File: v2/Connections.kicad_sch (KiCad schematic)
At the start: 11 parts, among them J3 Screw_Terminal_01x02, J4 Screw_Terminal_01x03, U10 TPD4E05U06DQA

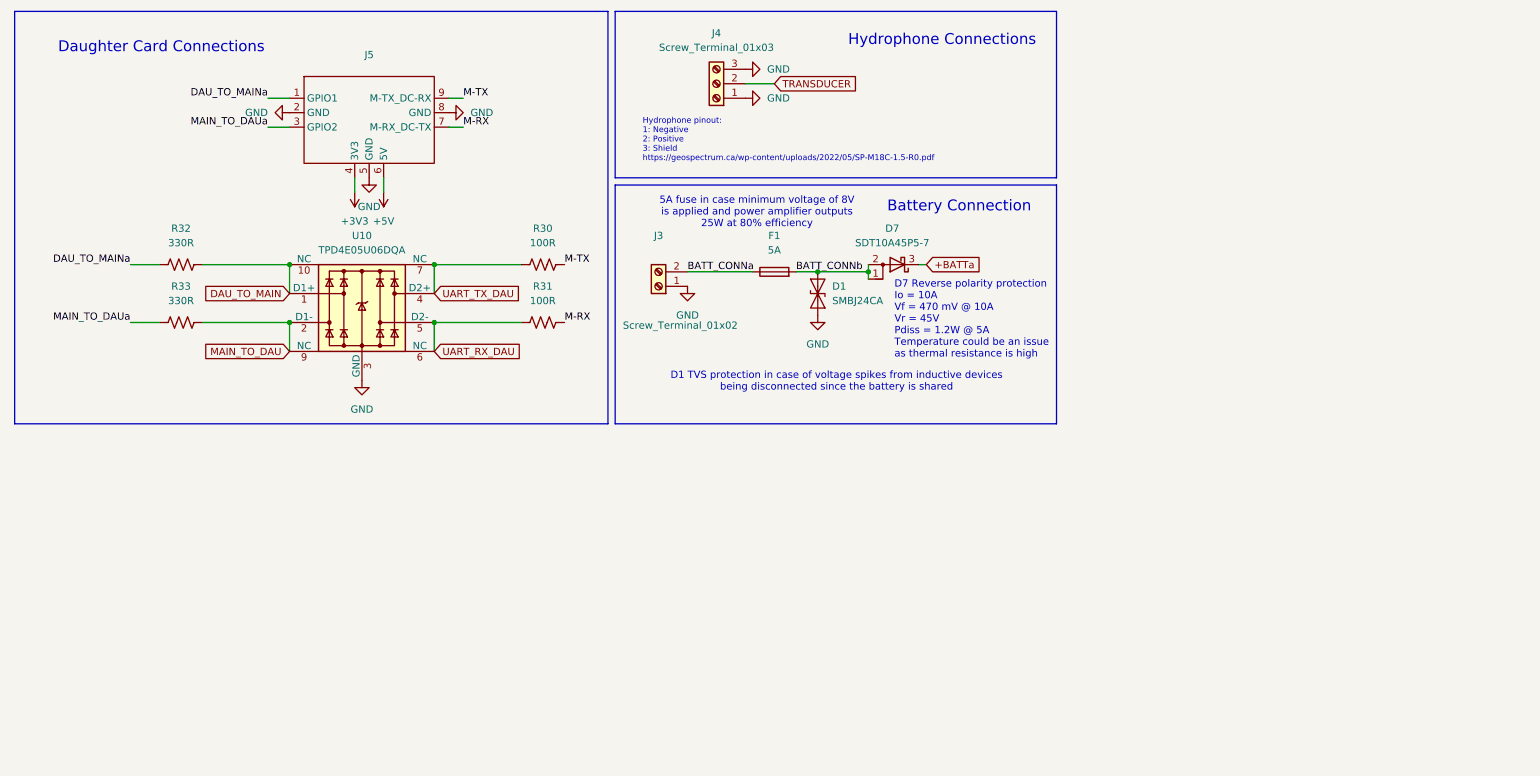
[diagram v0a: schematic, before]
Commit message: Most v2 changes made
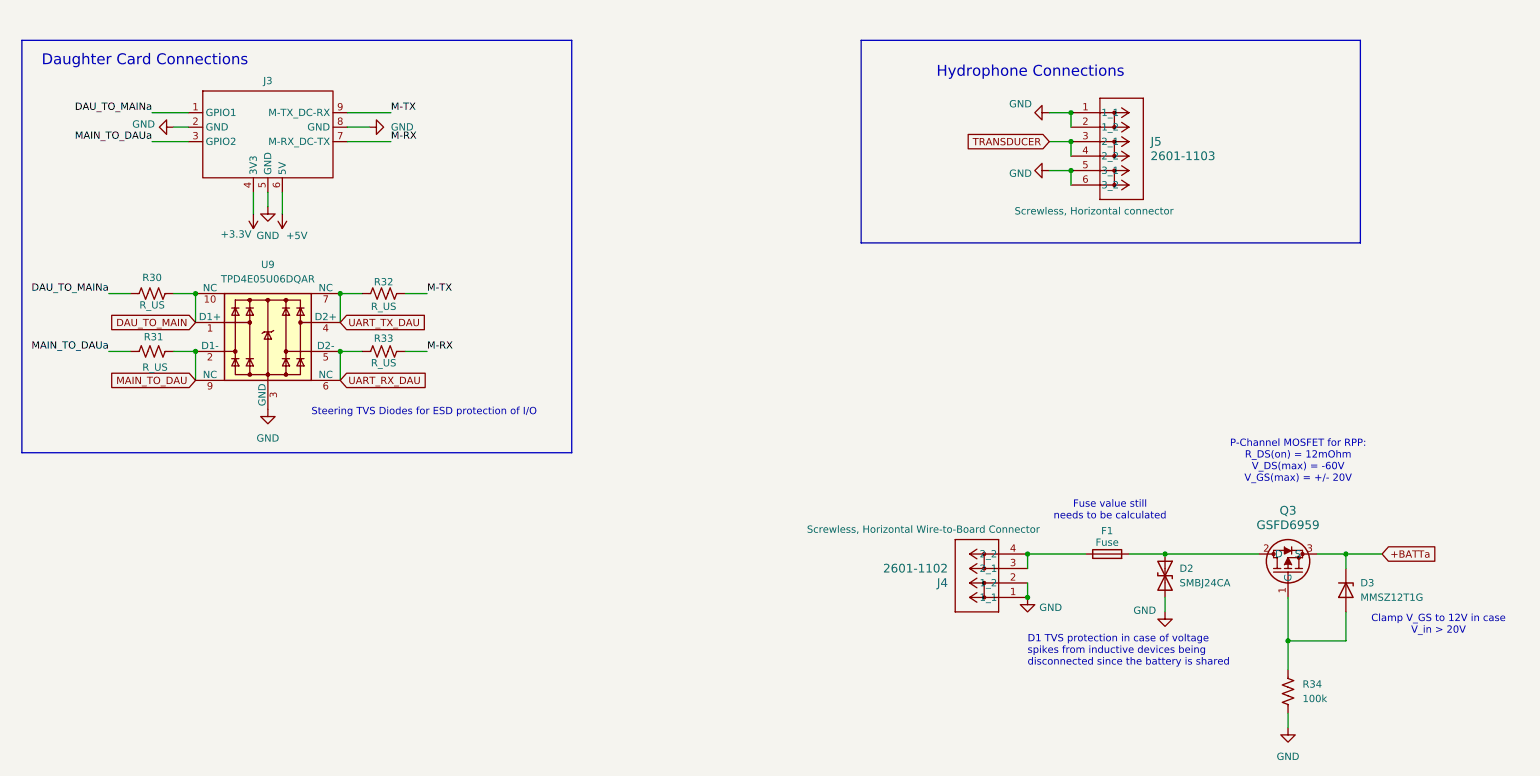
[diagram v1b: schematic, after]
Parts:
- removed D1: SMBJ24CA, Diode_SMD:D_SMA, symbol UAM_symbols:SMAJ24CA
- removed D7: SDT10A45P5-7, Diodes:PowerDI-5, symbol UAM_symbols:D_Schottky_AAK
- removed J3: Screw_Terminal_01x02, TerminalBlock:TerminalBlock_Xinya_XY308-2.54-2P_1x02_P2.54mm_Horizontal, symbol UAM_symbols:Screw_Terminal_01x02
- removed J4: Screw_Terminal_01x03, TerminalBlock:TerminalBlock_Xinya_XY308-2.54-3P_1x03_P2.54mm_Horizontal, symbol UAM_symbols:Screw_Terminal_01x03
- removed J5: ~, Connections:UAM_DaughterCard, symbol UAM_symbols:UAM_DaughterCard
- removed R30, R31: 100R, Resistor_SMD:R_0603_1608Metric_Pad0.98x0.95mm_HandSolder, symbol UAM_symbols:R_US
- removed R32, R33: 330R, Resistor_SMD:R_0603_1608Metric_Pad0.98x0.95mm_HandSolder, symbol UAM_symbols:R_US
- removed U10: TPD4E05U06DQA, Package_SON:USON-10_2.5x1.0mm_P0.5mm, symbol UAM_symbols:TPD4E05U06DQA
- added D2: SMBJ24CA, UAM_footprints:SMBJ, symbol Device:D_TVS
- added D3: MMSZ12T1G, UAM_footprints:SOD-123_ONS, symbol Device:D_Zener
- added J3: ~, symbol UAM_symbols:UAM_DaughterCard
- added J4: 2601-1102, UAM_footprints:CONN2_2601-1102_WAG, symbol UAM_symbols:2601-1102
- added J5: 2601-1103, UAM_footprints:CONN3_2601-1103_WAG, symbol UAM_symbols:2601-1103
- added Q3: GSFD6959, UAM_footprints:PMOSGDS_TO-252_DPAK_GAS, symbol UAM_symbols:GSFD6959
- added R30, R31, R32, R33: R_US, symbol Device:R_US
- added R34: 100k, symbol Device:R_US
- added U9: TPD4E05U06DQAR, Package_SON:USON-10_2.5x1.0mm_P0.5mm, symbol UAM_symbols:TPD4E05U06DQA
- F1: value 5A -> Fuse; footprint Fuse:Fuse_0603_1608Metric_Pad1.05x0.95mm_HandSolder -> (none)
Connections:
- net +5V: now also J3.6 (5V)
- net +BATTa: now also D3.1 (K), Q3.3 (S)
- net DAU_TO_MAIN: now also R30.2, U9.1 (D1+), U9.10 (NC)
- net DAU_TO_MAINa: now also J3.1 (GPIO1), R30.1
- net GND: now also D2.2 (A2), J3.2 (GND), J3.5 (GND), J3.8 (GND), J4.1 (1_1), J4.2 (1_2), J5.1 (1_1), J5.2 (1_2), J5.5 (3_1), J5.6 (3_2), R34.2, U9.3 (GND), U9.8 (GND)
- net M-RX: now also J3.7 (M-RX_DC-TX), R33.2
- net M-TX: now also J3.9 (M-TX_DC-RX), R32.2
- net MAIN_TO_DAU: now also R31.2, U9.2 (D1-), U9.9 (NC)
- net MAIN_TO_DAUa: now also J3.3 (GPIO2), R31.1
- net TRANSDUCER: now also J5.3 (2_1), J5.4 (2_2)
- net UART_RX_DAU: now also R33.1, U9.5 (D2-), U9.6 (NC)
- net UART_TX_DAU: now also R32.1, U9.4 (D2+), U9.7 (NC)
- net BATT_CONNa: no longer names the net of F1.1
- net BATT_CONNa: now also J4.3 (2_1), J4.4 (2_2)
- net BATT_CONNb: no longer names the net of F1.2
- net BATT_CONNb: now also D2.1 (A1), Q3.2 (D)
- new net: D3.2 (A), Q3.1 (G), R34.1
- new net +3.3V: J3.4 (3V3)
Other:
- note added: "Clamp V_GS to 12V in case V_in > 20V"
- note added: "Fuse value still needs to be calculated"
- note added: "P-Channel MOSFET for RPP: R_DS(on) = 12mOhm V_DS(max) = -60V V_GS(max) = +/- 20V"
- note added: "Steering TVS Diodes for ESD protection of I/O"
- note removed: "5A fuse in case minimum voltage of 8V is applied and power amplifier outputs 25W at 80% efficiency"
- note removed: "Battery Connection"
- note removed: "D7 Reverse polarity protection Io = 10A Vf = 470 mV @ 10A Vr = 45V Pdiss = 1.2W @ 5A Temperature could be an issue as thermal resistance is high"
- note removed: "Hydrophone pinout: 1: Negative 2: Positive 3: Shield https://geospectrum.ca/wp-content/uploads/2022/05/SP-M18C-1.5-R0.pdf"
- company: External Connections -> (none)
- title: EV -> External Connections to Main Board
